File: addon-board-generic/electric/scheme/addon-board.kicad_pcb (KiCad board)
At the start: 2 copper layers, 85 x 56 mm, 66 parts, among them K1 CONN_3, K2 CONN_3, K3 CONN_3, K4 CONN_3, K5 CONN_3, K6 CONN_3, K7 CONN_3, K8 CONN_3, P1 TST, P10 CONN_8, P11 CONN_10, P12 CONN_4, P13 CONN_4, P2 TST, P3 cross board conn, P4 cross board conn, P5 TST, P6 TST, P7 TST, P8 TST, P9 CONN_4, Q1 NPN, Q2 MOS_P, Q3 BC847, Q4 BC847, Q5 MOS_P, Q6 MOS_P, U1 L293, U2 L293, U3 74HC165, U4 74HC595_MY, U5 74HC595_MY, X1 8MHz

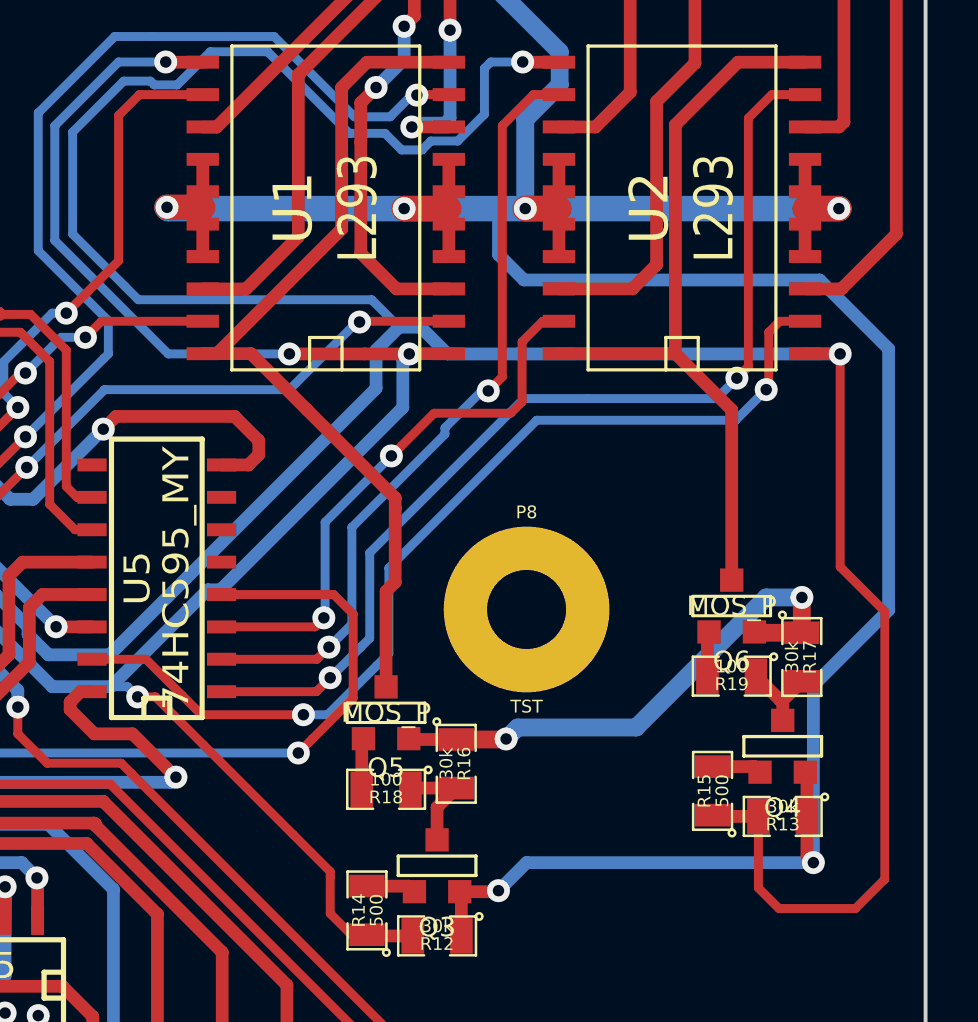
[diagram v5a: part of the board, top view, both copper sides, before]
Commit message: Added more ground viases.
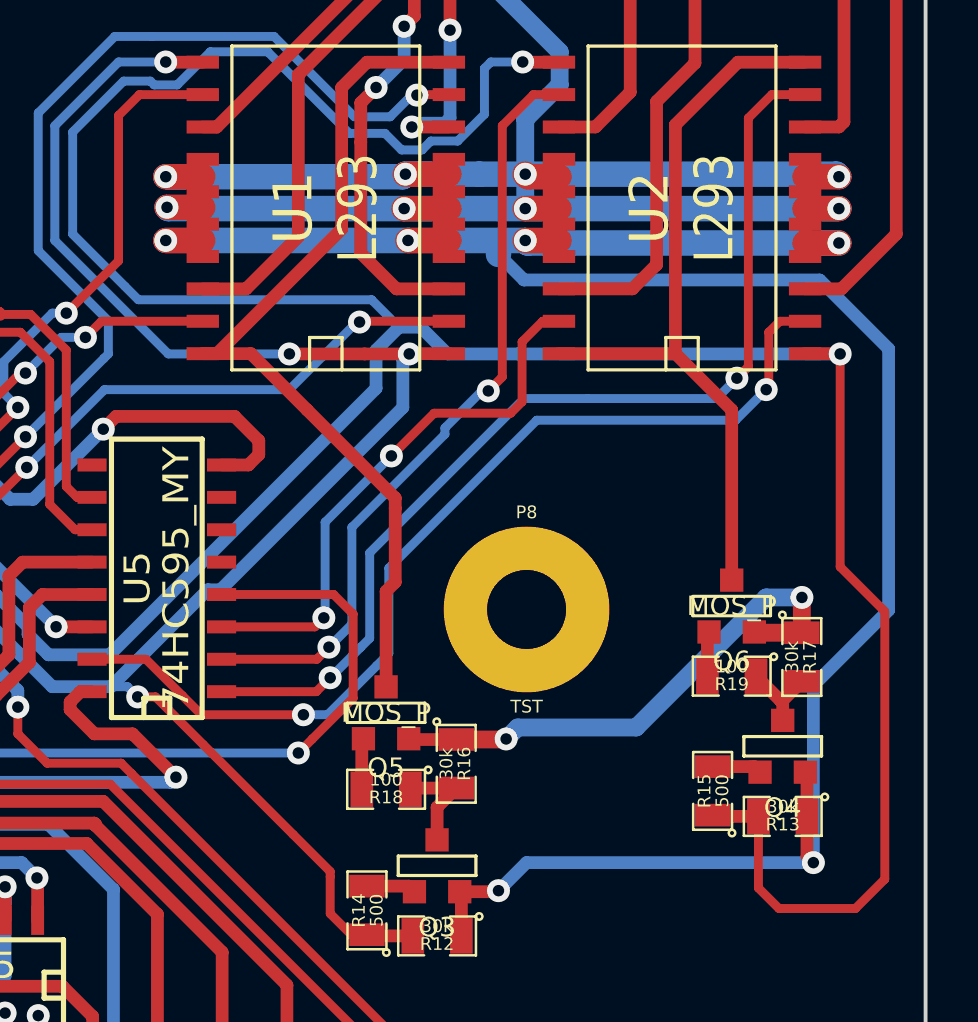
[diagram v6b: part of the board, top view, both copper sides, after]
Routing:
- net GND: track 538.0 -> 601.2 mm, vias 14 -> 22
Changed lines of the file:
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@@
     (thickness 1.6)
     (drawings 49)
-    (tracks 1201)
+    (tracks 1237)
     (zones 0)
     (modules 66)
@@
   )
   (setup
-    (last_trace_width 0.5)
+    (last_trace_width 1)
     (user_trace_width 0.35)
     (user_trace_width 0.5)
@@
   (segment (start 176.25 167.55) (end 176.25 167.95) (width 0.25) (layer F.Cu) (net 65))
   (segment (start 175.69828 166.99828) (end 176.25 167.55) (width 0.25) (layer F.Cu) (net 65))
+  (segment (start 211.75 142.5) (end 211.75 143.05) (width 1) (layer B.Cu) (net 66))
+  (segment (start 224.1 159.95) (end 227.05 157) (width 0.5) (layer B.Cu) (net 66))
+  (segment (start 227.05 157) (end 227.05 146.75) (width 0.5) (layer B.Cu) (net 66))
+  (segment (start 227.05 146.75) (end 224.35 144.05) (width 0.5) (layer B.Cu) (net 66))
+  (segment (start 224.35 144.05) (end 212.75 144.05) (width 0.5) (layer B.Cu) (net 66))
+  (segment (start 212.75 144.05) (end 211.75 143.05) (width 0.5) (layer B.Cu) (net 66))
+  (segment (start 224.1 159.95) (end 224.1 166.9) (width 0.5) (layer B.Cu) (net 66))
+  (segment (start 208.2 142.5) (end 211.75 142.5) (width 1) (layer B.Cu) (net 66))
+  (segment (start 211.75 142.5) (end 212.8 142.5) (width 1) (layer B.Cu) (net 66))
+  (segment (start 214.122 142.5) (end 212.8 142.5) (width 1) (layer F.Cu) (net 66))
+  (via (at 212.8 142.5) (size 0.9) (layers F.Cu B.Cu) (net 66))
+  (segment (start 225.1 142.6) (end 223.774 142.6) (width 1) (layer F.Cu) (net 66))
+  (segment (start 212.8 142.5) (end 212.9 142.6) (width 1) (layer B.Cu) (net 66))
+  (segment (start 212.9 142.6) (end 225.1 142.6) (width 1) (layer B.Cu) (net 66))
+  (via (at 225.1 142.6) (size 0.9) (layers F.Cu B.Cu) (net 66))
+  (segment (start 200.152 142.5) (end 198.7 142.5) (width 1) (layer F.Cu) (net 66))
+  (segment (start 208.2 142.5) (end 209.804 142.5) (width 1) (layer F.Cu) (net 66))
+  (via (at 208.2 142.5) (size 0.9) (layers F.Cu B.Cu) (net 66))
+  (segment (start 198.7 142.5) (end 208.2 142.5) (width 1) (layer B.Cu) (net 66))
+  (via (at 198.7 142.5) (size 0.9) (layers F.Cu B.Cu) (net 66))
+  (via (at 208.1 139.9) (size 0.9) (layers F.Cu B.Cu) (net 66))
+  (segment (start 208.1 139.9) (end 209.804 139.9) (width 1) (layer F.Cu) (net 66))
+  (via (at 198.7 140) (size 0.9) (layers F.Cu B.Cu) (net 66))
+  (segment (start 211 139.9) (end 208.1 139.9) (width 1) (layer B.Cu) (net 66))
+  (segment (start 208.1 139.9) (end 208 140) (width 1) (layer B.Cu) (net 66))
+  (segment (start 208 140) (end 198.7 140) (width 1) (layer B.Cu) (net 66))
+  (segment (start 212.8 139.9) (end 211 139.9) (width 1) (layer B.Cu) (net 66))
+  (segment (start 198.7 140) (end 200.152 140) (width 1) (layer F.Cu) (net 66))
+  (segment (start 223.774 140) (end 225.1 140) (width 1) (layer F.Cu) (net 66))
+  (segment (start 212.9 140) (end 214.122 140) (width 1) (layer F.Cu) (net 66))
+  (segment (start 212.8 139.9) (end 212.9 140) (width 1) (layer F.Cu) (net 66))
+  (via (at 212.8 139.9) (size 0.9) (layers F.Cu B.Cu) (net 66))
+  (segment (start 225 139.9) (end 212.8 139.9) (width 1) (layer B.Cu) (net 66))
+  (segment (start 225.1 140) (end 225 139.9) (width 1) (layer B.Cu) (net 66))
+  (via (at 225.1 140) (size 0.9) (layers F.Cu B.Cu) (net 66))
   (segment (start 173.736 127.254) (end 173.736 127.836) (width 1) (layer B.Cu) (net 66))
   (segment (start 175.2 129.3) (end 175.2 131.2) (width 1) (layer B.Cu) (net 66))
@@
   (segment (start 151.75 129) (end 150.876 128.126) (width 1) (layer B.Cu) (net 66))
   (segment (start 150.876 128.126) (end 150.876 127.254) (width 1) (layer B.Cu) (net 66))
-  (segment (start 224.1 166.9) (end 224.1 159.95) (width 0.5) (layer B.Cu) (net 66))
-  (segment (start 211.75 143.05) (end 211.75 141.25) (width 0.5) (layer B.Cu) (net 66))
-  (segment (start 212.75 144.05) (end 211.75 143.05) (width 0.5) (layer B.Cu) (net 66))
-  (segment (start 224.35 144.05) (end 212.75 144.05) (width 0.5) (layer B.Cu) (net 66))
-  (segment (start 227.05 146.75) (end 224.35 144.05) (width 0.5) (layer B.Cu) (net 66))
-  (segment (start 227.05 157) (end 227.05 146.75) (width 0.5) (layer B.Cu) (net 66))
-  (segment (start 224.1 159.95) (end 227.05 157) (width 0.5) (layer B.Cu) (net 66))
   (segment (start 169.4 166.25) (end 169.75 166.25) (width 0.25) (layer F.Cu) (net 66))
   (segment (start 170.2479 166.7479) (end 170.2479 168.34702) (width 0.25) (layer F.Cu) (net 66))
@@
   (segment (start 181.25 135.05) (end 180.95 135.05) (width 0.7) (layer B.Cu) (net 66))
   (segment (start 210.231 168.04) (end 211.71 168.04) (width 0.5) (layer F.Cu) (net 66))
+  (segment (start 211.71 168.04) (end 211.75 168) (width 0.5) (layer F.Cu) (net 66))
+  (via (at 211.75 168) (size 0.9) (layers F.Cu B.Cu) (net 66))
+  (segment (start 211.75 168) (end 212.85 166.9) (width 0.5) (layer B.Cu) (net 66))
+  (segment (start 212.85 166.9) (end 224.1 166.9) (width 0.5) (layer B.Cu) (net 66))
   (segment (start 223.8495 166.6495) (end 223.8495 165.087) (width 0.5) (layer F.Cu) (net 66))
-  (segment (start 224.1 166.9) (end 223.8495 166.6495) (width 0.5) (layer F.Cu) (net 66))
   (via (at 224.1 166.9) (size 0.9) (layers F.Cu B.Cu) (net 66))
-  (segment (start 212.85 166.9) (end 224.1 166.9) (width 0.5) (layer B.Cu) (net 66))
-  (segment (start 211.75 168) (end 212.85 166.9) (width 0.5) (layer B.Cu) (net 66))
-  (via (at 211.75 168) (size 0.9) (layers F.Cu B.Cu) (net 66))
-  (segment (start 211.71 168.04) (end 211.75 168) (width 0.5) (layer F.Cu) (net 66))
+  (segment (start 224.1 166.9) (end 223.8495 166.6495) (width 0.5) (layer F.Cu) (net 66))
   (segment (start 166.116 127.254) (end 166.116 127.584) (width 1) (layer B.Cu) (net 66))
   (segment (start 182.3 132.7) (end 182.3 133.7) (width 1) (layer B.Cu) (net 66))
@@
   (segment (start 198.75 141.2) (end 198.8 141.25) (width 1) (layer B.Cu) (net 66))
   (via (at 198.75 141.2) (size 0.9) (layers F.Cu B.Cu) (net 66))
-  (segment (start 200.152 140.589) (end 200.152 139.319) (width 0.5) (layer F.Cu) (net 66))
+  (segment (start 200.152 140.589) (end 200.152 140) (width 0.5) (layer F.Cu) (net 66))
+  (segment (start 200.152 140) (end 200.152 139.319) (width 0.5) (layer F.Cu) (net 66))
   (segment (start 200.152 141.859) (end 200.152 141.2) (width 0.5) (layer F.Cu) (net 66))
   (segment (start 200.152 141.2) (end 200.152 140.589) (width 0.5) (layer F.Cu) (net 66))
-  (segment (start 200.152 143.129) (end 200.152 141.859) (width 0.5) (layer F.Cu) (net 66))
-  (segment (start 223.774 140.589) (end 223.774 139.319) (width 0.5) (layer F.Cu) (net 66))
+  (segment (start 200.152 143.129) (end 200.152 142.5) (width 0.5) (layer F.Cu) (net 66))
+  (segment (start 200.152 142.5) (end 200.152 141.859) (width 0.5) (layer F.Cu) (net 66))
+  (segment (start 223.774 140.589) (end 223.774 140) (width 0.5) (layer F.Cu) (net 66))
+  (segment (start 223.774 140) (end 223.774 139.319) (width 0.5) (layer F.Cu) (net 66))
   (segment (start 223.774 141.859) (end 223.774 141.25) (width 0.5) (layer F.Cu) (net 66))
   (segment (start 223.774 141.25) (end 223.774 140.589) (width 0.5) (layer F.Cu) (net 66))
-  (segment (start 223.774 143.129) (end 223.774 141.859) (width 0.5) (layer F.Cu) (net 66))
-  (segment (start 214.122 140.589) (end 214.122 139.319) (width 0.5) (layer F.Cu) (net 66))
+  (segment (start 223.774 143.129) (end 223.774 142.6) (width 0.5) (layer F.Cu) (net 66))
+  (segment (start 223.774 142.6) (end 223.774 141.859) (width 0.5) (layer F.Cu) (net 66))
+  (segment (start 214.122 140.589) (end 214.122 140) (width 0.5) (layer F.Cu) (net 66))
+  (segment (start 214.122 140) (end 214.122 139.319) (width 0.5) (layer F.Cu) (net 66))
   (segment (start 214.122 141.859) (end 214.122 141.25) (width 0.5) (layer F.Cu) (net 66))
   (segment (start 214.122 141.25) (end 214.122 140.589) (width 0.5) (layer F.Cu) (net 66))
-  (segment (start 214.122 143.129) (end 214.122 141.859) (width 0.5) (layer F.Cu) (net 66))
-  (segment (start 209.804 141.859) (end 209.804 143.129) (width 0.5) (layer F.Cu) (net 66))
+  (segment (start 214.122 143.129) (end 214.122 142.5) (width 0.5) (layer F.Cu) (net 66))
+  (segment (start 214.122 142.5) (end 214.122 141.859) (width 0.5) (layer F.Cu) (net 66))
+  (segment (start 209.804 141.859) (end 209.804 142.5) (width 0.5) (layer F.Cu) (net 66))
+  (segment (start 209.804 142.5) (end 209.804 143.129) (width 0.5) (layer F.Cu) (net 66))
   (segment (start 209.804 140.589) (end 209.804 141.25) (width 0.5) (layer F.Cu) (net 66))
   (segment (start 209.804 141.25) (end 209.804 141.859) (width 0.5) (layer F.Cu) (net 66))
-  (segment (start 209.804 139.319) (end 209.804 140.589) (width 0.5) (layer F.Cu) (net 66))
+  (segment (start 209.804 139.319) (end 209.804 139.9) (width 0.5) (layer F.Cu) (net 66))
+  (segment (start 209.804 139.9) (end 209.804 140.589) (width 0.5) (layer F.Cu) (net 66))
   (segment (start 172.75 160.2025) (end 173.4975 160.2025) (width 0.35) (layer F.Cu) (net 66))
   (segment (start 176.15 152.498) (end 176.146 152.494) (width 0.35) (layer F.Cu) (net 66))

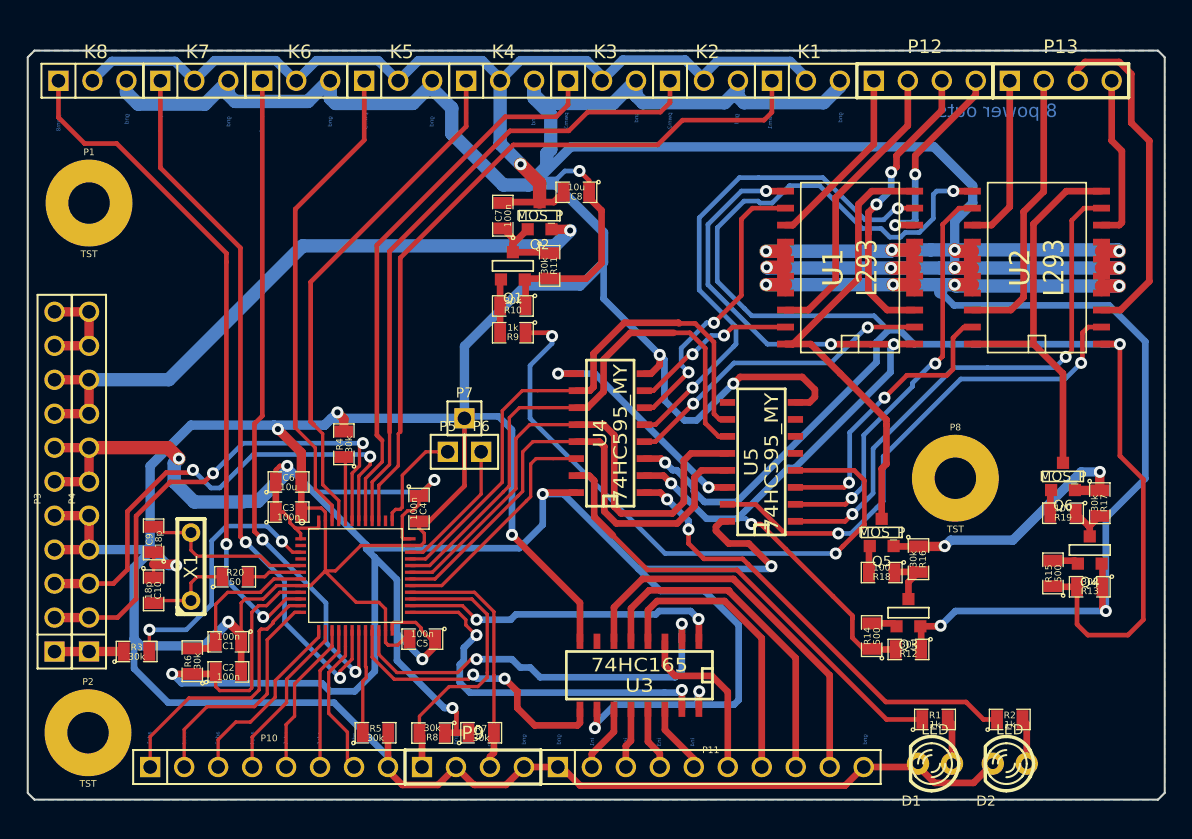
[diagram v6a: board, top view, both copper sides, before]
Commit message: Moved peripherial sockets closer to outer board edge.
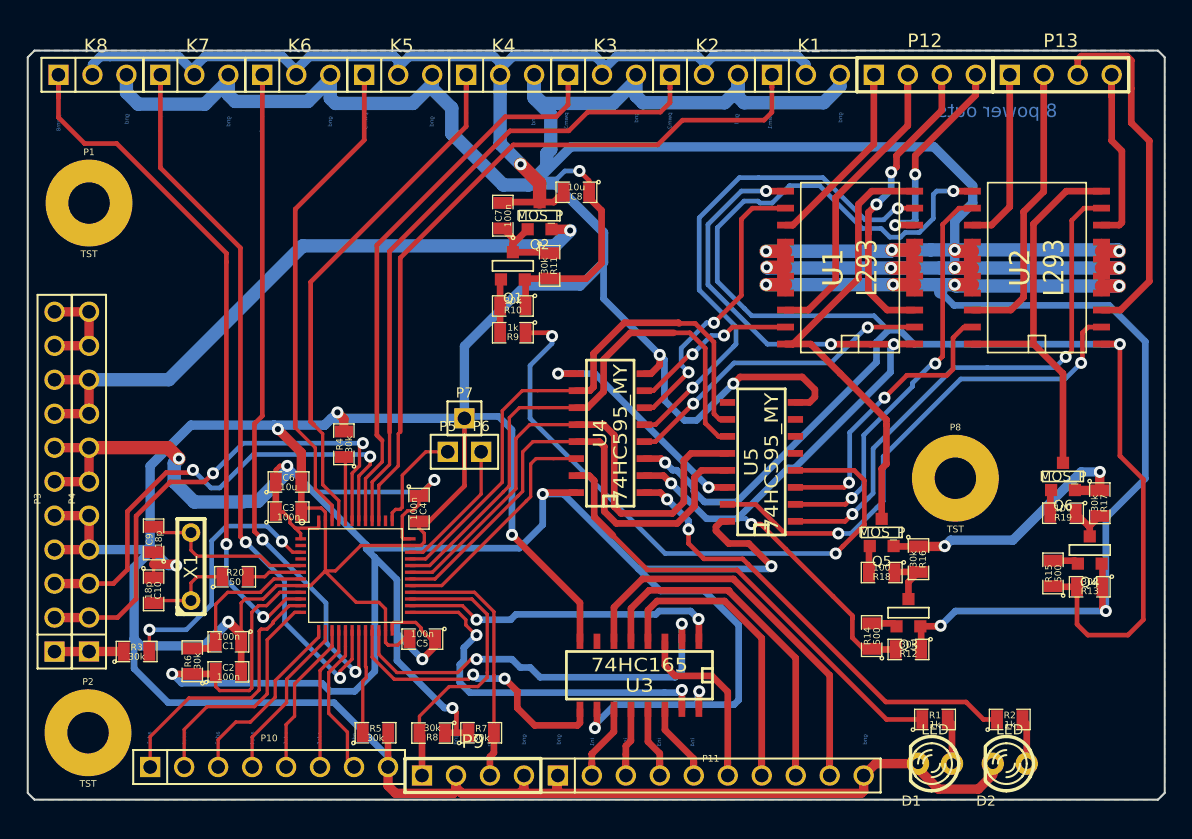
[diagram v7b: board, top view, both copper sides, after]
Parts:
- moved P11 0.63 mm to (194.6, 179.2)
- moved P9 0.63 mm to (176.8, 179.2)
- moved K1 0.44 mm to (201.7, 126.8)
- moved K2 0.44 mm to (194.1, 126.8)
- moved K3 0.44 mm to (186.4, 126.8)
- moved K4 0.44 mm to (178.8, 126.8)
- moved K5 0.44 mm to (171.2, 126.8)
- moved K6 0.44 mm to (163.6, 126.8)
- moved K7 0.44 mm to (156.0, 126.8)
- moved K8 0.44 mm to (148.3, 126.8)
- moved P12 0.44 mm to (210.6, 126.8)
- moved P13 0.44 mm to (220.7, 126.8)
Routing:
- net GND: track 601.2 -> 608.5 mm
- net /servo-vdd+: track 78.0 -> 83.6 mm
- net /servo8: track 51.2 -> 52.9 mm
- net /in1: track 7.38 -> 8.96 mm
- net /in0: track 9.02 -> 10.6 mm
- net /out6: track 12.5 -> 14.1 mm
- net /servo4: track 38.6 -> 39.9 mm
- net /servo7: track 54.1 -> 55.3 mm
- net /out4: track 21.9 -> 23.1 mm
- net /servo6: track 50.8 -> 51.9 mm
- net /out8: track 21.0 -> 22.2 mm
- net /out3: track 13.9 -> 15.0 mm
- net /in7: track 29.4 -> 30.5 mm
- net /in2: track 4.69 -> 5.83 mm
- net /servo5: track 36.2 -> 37.3 mm
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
